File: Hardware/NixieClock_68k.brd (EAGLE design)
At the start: 100 x 100 mm, 70 parts, among them IC1 68008, IC10 7805, IC11 MIC803, IC2 AS6C1008, IC3 39SF020, IC4 DS1244Y, IC5 FT245R, IC6 NE555, IC7 ATF1504AS, IC8 74HC374N, IC9 74HC373N, X1 4MHz

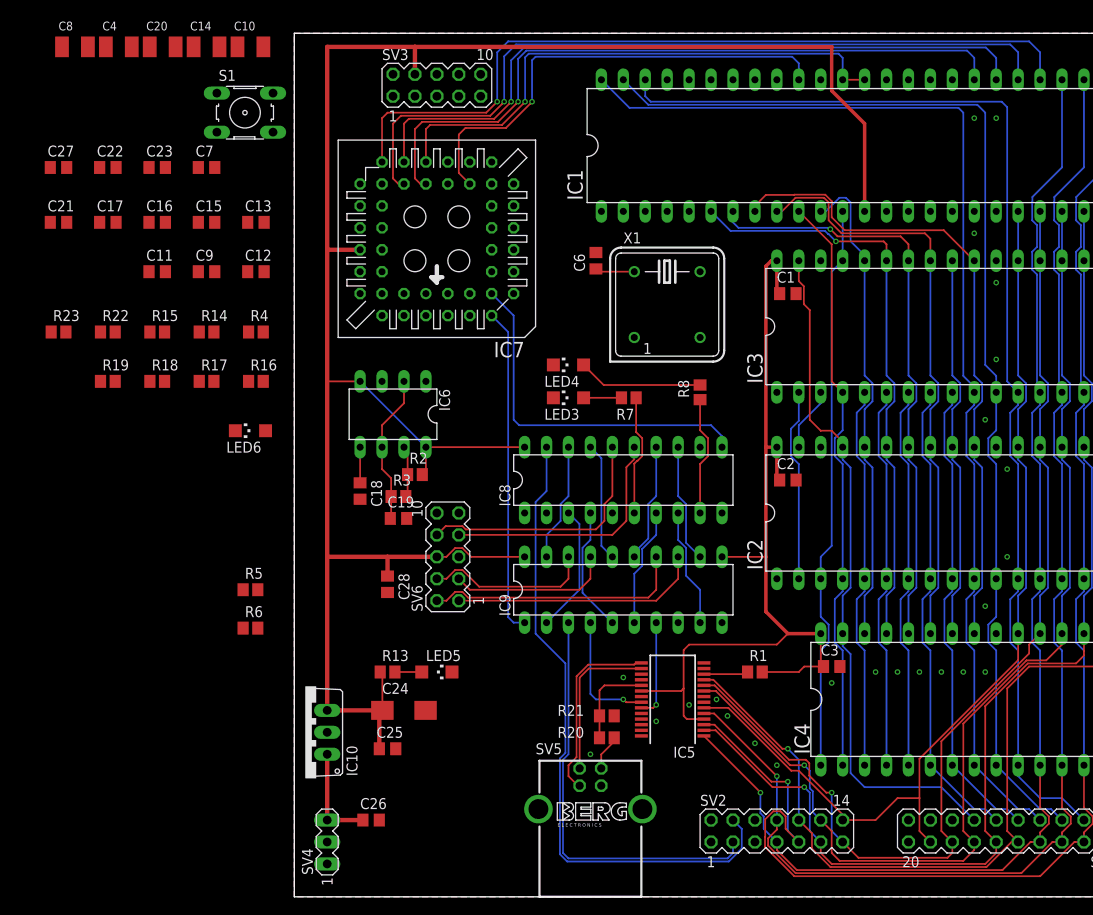
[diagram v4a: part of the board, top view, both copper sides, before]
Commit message: replaced cpld with ttl logic
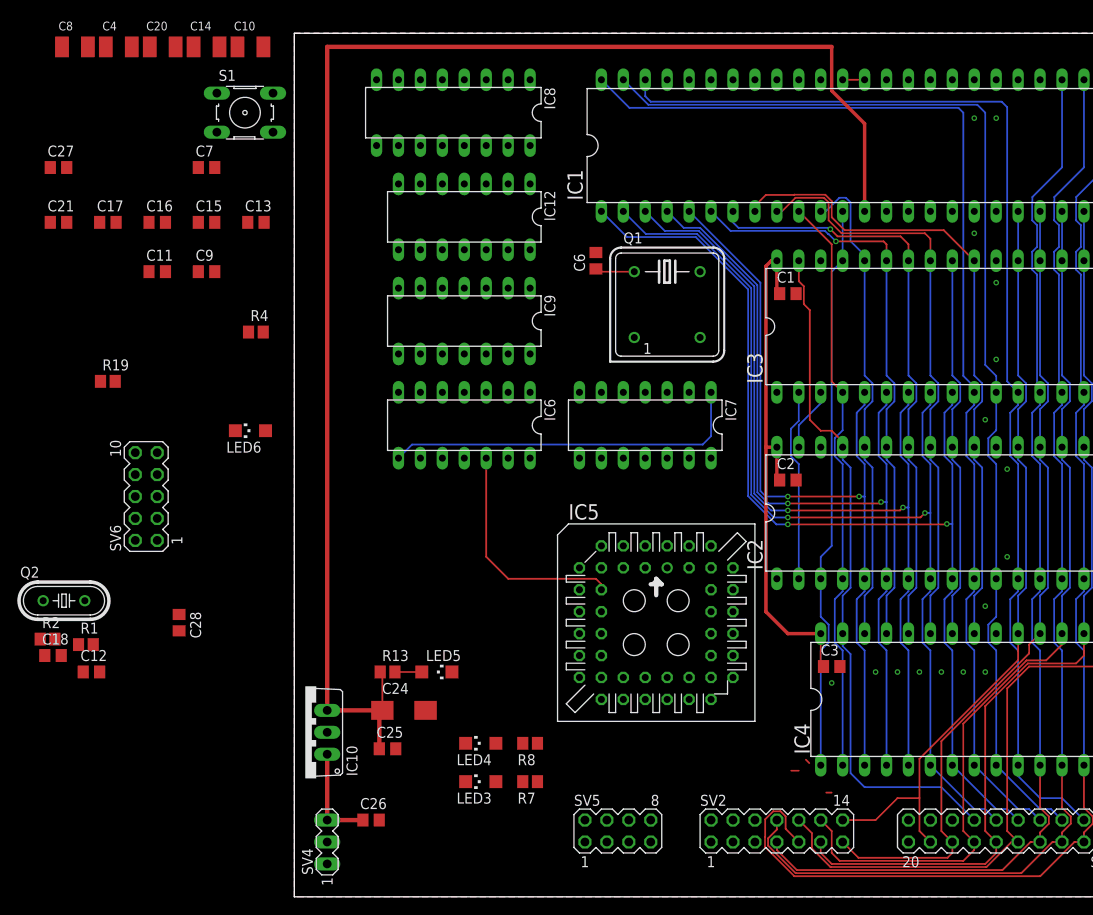
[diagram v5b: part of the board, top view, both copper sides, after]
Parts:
- removed C19: 47nF, rcl:C0805
- removed C22, C23: 100nF, rcl:C0805
- removed R14, R15, R16, R17, R18, R21, R22, R23, R5, R6: 10k, rcl:R2012
- removed R20: 4k7, rcl:R2012
- removed R3: 150k, rcl:R2012
- removed SV3: (no value), con-lstb:MA05-2
- added IC12: 74HC08N, 74xx-eu:DIL14
- added Q2: 3.6864MHz, crystal:HC49/S
- C12: value 100nF -> 27pF
- C18: value 10nF -> 27pF
- IC5: value FT245R -> 68681; device Parts:SSOP28 -> Parts:PLCC-S44
- IC6: value NE555 -> 74HC30N; device st-microelectronics:DIL-08 -> 74xx-eu:DIL14
- IC7: value ATF1504AS -> 74HC04N; device Parts:PLCC-S44 -> 74xx-eu:DIL14
- IC8: value 74HC374N -> 74HC138N; device 74xx-eu:DIL20 -> 74xx-eu:DIL16
- IC9: value 74HC373N -> 74HC266N; device 74xx-eu:DIL20 -> 74xx-eu:DIL14
- R1: value 10k -> 100R
- R2: value 4k7 -> 100R
- SV5: value PN61729-S -> (none); device con-berg:PN61729-S -> con-lstb:MA04-2
- moved R1 77.5 mm to (-24.1, 29.2)
- moved C12 50.1 mm to (-23.5, 26.0)
- moved IC8 46.9 mm to (18.4, 90.8), turned to 180 degrees
- moved R2 46.6 mm to (-28.6, 29.8)
- moved R7 45.9 mm to (27.3, 13.3)
- moved LED3 45.6 mm to (21.6, 13.3)
- moved R8 45.2 mm to (27.3, 17.8), turned to 180 degrees
- moved LED4 45.0 mm to (21.6, 17.8)
- moved C18 40.3 mm to (-27.9, 27.9), turned to 0 degrees
- moved IC9 36.2 mm to (19.7, 66.7), turned to 180 degrees
- moved SV6 35.6 mm to (-17.1, 46.4)
- moved IC7 32.4 mm to (40.6, 54.6)
- moved C28 24.5 mm to (-13.3, 31.8)
- moved IC5 9.09 mm to (41.9, 31.8), turned to 0 degrees
- moved IC6 8.35 mm to (19.7, 54.6)
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- renumbered X1 to Q1
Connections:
- removed net !BERR: IC1.40, R14.1
- removed net !BR: IC1.33, R18.1
- removed net !IO_IN_CS: IC7.6, IC9.1
- removed net !IO_OUT_CS: IC7.8, IC8.11
- removed net !USB_PWREN: IC5.12, R1.1
- removed net !USB_RD: IC5.13
- removed net !USB_RESET: IC5.19, R20.1, R21.2
- removed net !USB_RXF: IC5.23, IC9.7, R6.1
- removed net !USB_TXE: IC5.22, IC9.4, R5.1
- removed net !VFD_WR: SV2.5
- removed net !VPA: IC1.39, IC7.21, R22.1
- removed net 555_D: IC6.7, R2.1, R3.2
- removed net 555_T: C19.1, IC6.2, IC6.6, R3.1
- removed net CPLD_TCK: IC7.32, R17.1, SV3.1
- removed net CPLD_TDI: IC7.7, R16.1, SV3.9
- removed net CPLD_TDO: IC7.38, SV3.3
- removed net CPLD_TMS: IC7.13, R15.1, SV3.5
- removed net N$10: R20.2, SV5.1
- removed net N$12: IC7.18
- removed net N$13: IC7.19
- removed net N$14: IC7.20
- removed net N$21: IC7.29
- removed net N$22: IC7.31
- removed net N$23: IC7.33
- removed net N$24: IC7.34
- removed net N$25: IC7.36
- removed net N$26: IC7.37
- removed net N$27: IC7.39
- removed net N$28: IC7.40
- removed net N$29: IC7.1
- removed net N$30: IC7.44
- removed net N$31: IC7.41
- removed net N$32: IC7.4
- removed net N$33: IC7.5
- removed net N$36: IC7.9
- removed net N$37: IC7.11
- removed net N$38: IC7.12
- removed net TIMER_IRQ: IC6.3
- removed net USB+: IC5.15, SV5.3
- removed net USB-: IC5.16, SV5.2
- removed net USB_WR: IC5.14
- new net !68681_CS: IC5.39, IC8.13
- new net !68681_DTACK: IC5.10, IC6.12
- new net !68681_IACK: IC5.41, IC7.6
- new net !RAM_CS0: IC8.9, IC9.5
- new net !RAM_CS1: IC8.7, IC9.6
- new net !ROM_CS0: IC8.15, IC9.1
- new net !ROM_CS1: IC8.14, IC9.2
- new net !VFD_CS: IC6.11, IC8.10, SV2.5
- new net 68681_X1: IC5.36, R2.1
- new net 68681_X2: IC5.37, R1.2
- new net UART0_RX: IC5.35, SV5.2
- new net UART0_TX: IC5.33, SV5.1
- new net UART1_RX: IC5.11, SV5.4
- new net UART1_TX: IC5.13, SV5.3
- net !AS: now also IC8.5; no longer IC7.28
- net !DS: no longer IC7.27
- net !DTACK: now also IC7.2; no longer IC7.25, R23.1
- net !IPL1: now also IC5.24
- net !NIXIE_CS: now also IC6.3, IC8.11
- net !OE: now also IC7.4
- net !RAM_CS: now also IC6.5, IC9.4
- net !RESET: now also IC5.38; no longer IC7.24
- net !ROM_CS: now also IC6.4, IC9.3
- net !RTC_CS: now also IC6.6, IC8.12
- net !VFD_RESET: now also IC5.30; no longer IC8.19
- net +5V: now also IC1.33, IC1.39, IC1.40, IC12.14, IC5.44, IC6.1, IC6.14, IC6.2, IC7.14, IC8.16, IC8.6, IC9.14, SV5.6, SV5.8; no longer C22.1, C23.1, IC5.20, IC5.4, IC6.4, IC6.8, IC7.15, IC7.23, IC7.3, IC7.35, IC8.20, IC9.11, IC9.20, R1.2, R14.2, R15.2, R16.2, R18.2, R2.2, R22.2, R23.2, R6.2, SV3.4
- net A0: now also IC5.2
- net A1: now also IC5.4
- net A16: now also IC8.1
- net A17: now also IC8.2
- net A18: now also IC8.3
- net A2: now also IC5.6
- net A3: now also IC5.7
- net CLK: no longer IC7.43
- net D0: now also IC5.28; no longer IC5.1, IC8.3, IC9.2
- net D1: now also IC5.18; no longer IC5.5, IC8.4, IC9.5
- net D2: now also IC5.27; no longer IC5.3, IC8.7, IC9.6
- net D3: now also IC5.19; no longer IC5.11, IC8.8, IC9.9
- net D4: now also IC5.26; no longer IC5.2, IC8.13, IC9.12
- net D5: now also IC5.20; no longer IC5.9, IC8.14, IC9.15
- net D6: now also IC5.25; no longer IC5.10, IC8.17, IC9.16
- net D7: now also IC5.21; no longer IC5.6, IC8.18, IC9.19
- net FC0: now also IC12.5
- net FC1: now also IC12.4
- net FC2: now also IC12.1
- net GND: now also C12.2, IC12.7, IC5.22, IC6.7, IC7.7, IC8.4, IC8.8, IC9.7, SV5.5, SV5.7; no longer C12.1, C19.2, C22.2, C23.2, IC5.18, IC5.21, IC5.25, IC5.26, IC5.7, IC6.1, IC7.10, IC7.22, IC7.30, IC7.42, IC8.1, IC8.10, IC9.10, IC9.8, R17.2, R21.1, R5.2, SV3.10, SV5.4, SV5.S1, SV5.S2
- net N$1: now also C12.1, Q2.2, R1.1; no longer C12.2, IC5.17
- net N$11: now also IC12.2, IC12.6; no longer IC7.14
- net N$2: now also Q2.1, R2.2; no longer IC6.5
- net N$3: now also IC6.8, IC7.1; no longer IC7.17
- net N$5: now also IC12.3, IC7.5; no longer IC7.16
- net OUT0: no longer IC8.16
- net OUT1: no longer IC8.15
- net R/!W!: now also IC5.9, IC7.3; no longer IC7.26
- net STATUS0: now also IC5.32; no longer IC8.2
- net STATUS1: now also IC5.14, R7.1; no longer IC8.5
- net STATUS2: now also IC5.31; no longer IC8.6, R7.1
- net STATUS3: now also IC5.15; no longer IC8.9
- net SW0: now also IC5.8; no longer IC9.13
- net SW1: now also IC5.5; no longer IC9.14
- net SW2: now also IC5.40; no longer IC9.17
- net SW3: now also IC5.43; no longer IC9.18
- net VFD_BUSY: now also IC5.3; no longer IC9.3
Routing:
- net +5V: track 340.9 -> 238.2 mm
- net !AS: track 92.0 -> 0.00 mm, vias 1 -> 0
- net !DS: track 90.7 -> 0.00 mm, vias 1 -> 0
- net R/!W!: track 163.7 -> 81.2 mm, vias 1 -> 0
- net !DTACK: track 81.6 -> 0.00 mm, vias 1 -> 0
- net !VFD_RESET: track 75.1 -> 0.00 mm
- net A3: track 54.9 -> 124.6 mm, vias 0 -> 2
- net A4: track 54.9 -> 119.4 mm, vias 0 -> 2
- net !RESET: track 64.0 -> 2.54 mm, vias 1 -> 0
- net A5: track 44.7 -> 103.7 mm, vias 0 -> 2
- net !VPA: track 54.4 -> 0.00 mm, vias 1 -> 0
- net A6: track 44.7 -> 98.2 mm, vias 0 -> 2
- net VFD_BUSY: track 48.4 -> 0.00 mm
- net A7: track 44.7 -> 92.8 mm, vias 0 -> 2
- net N$3: track 0.00 -> 42.3 mm
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
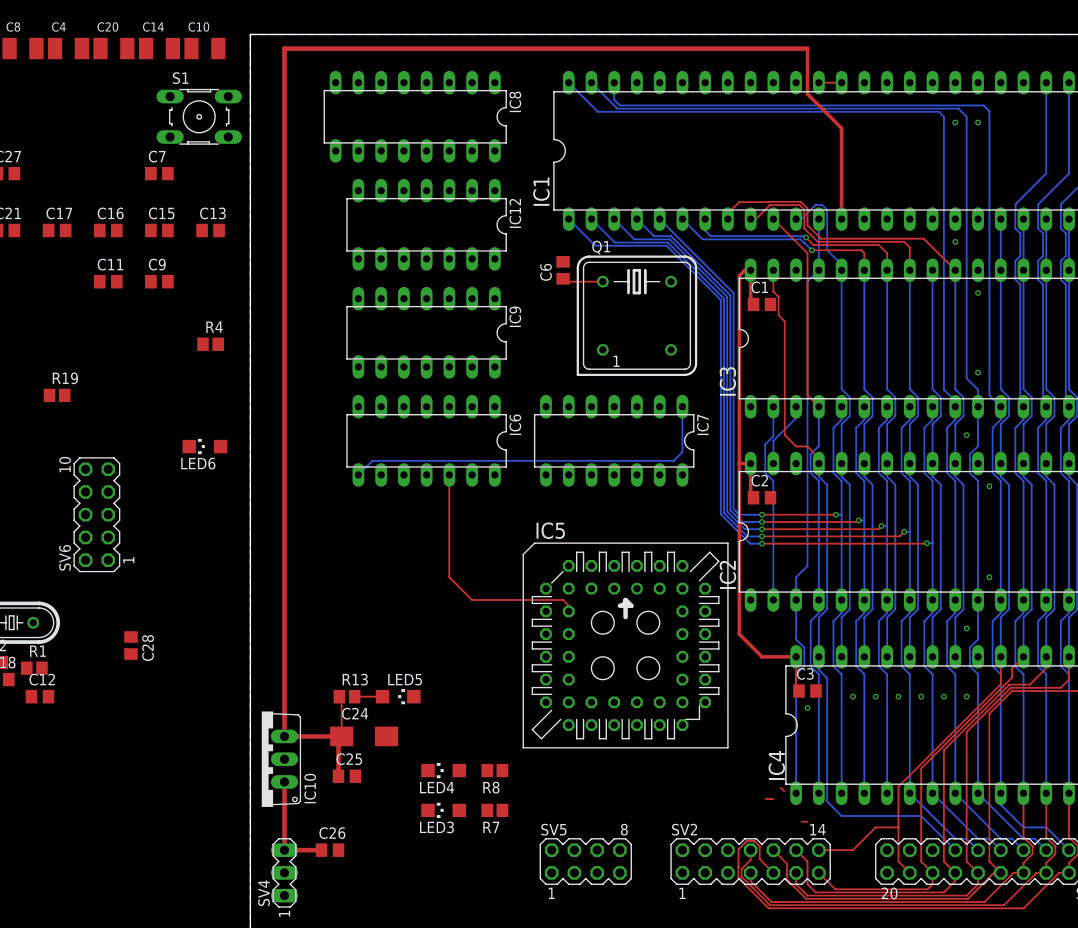
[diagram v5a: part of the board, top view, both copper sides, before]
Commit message: routed most system control signals
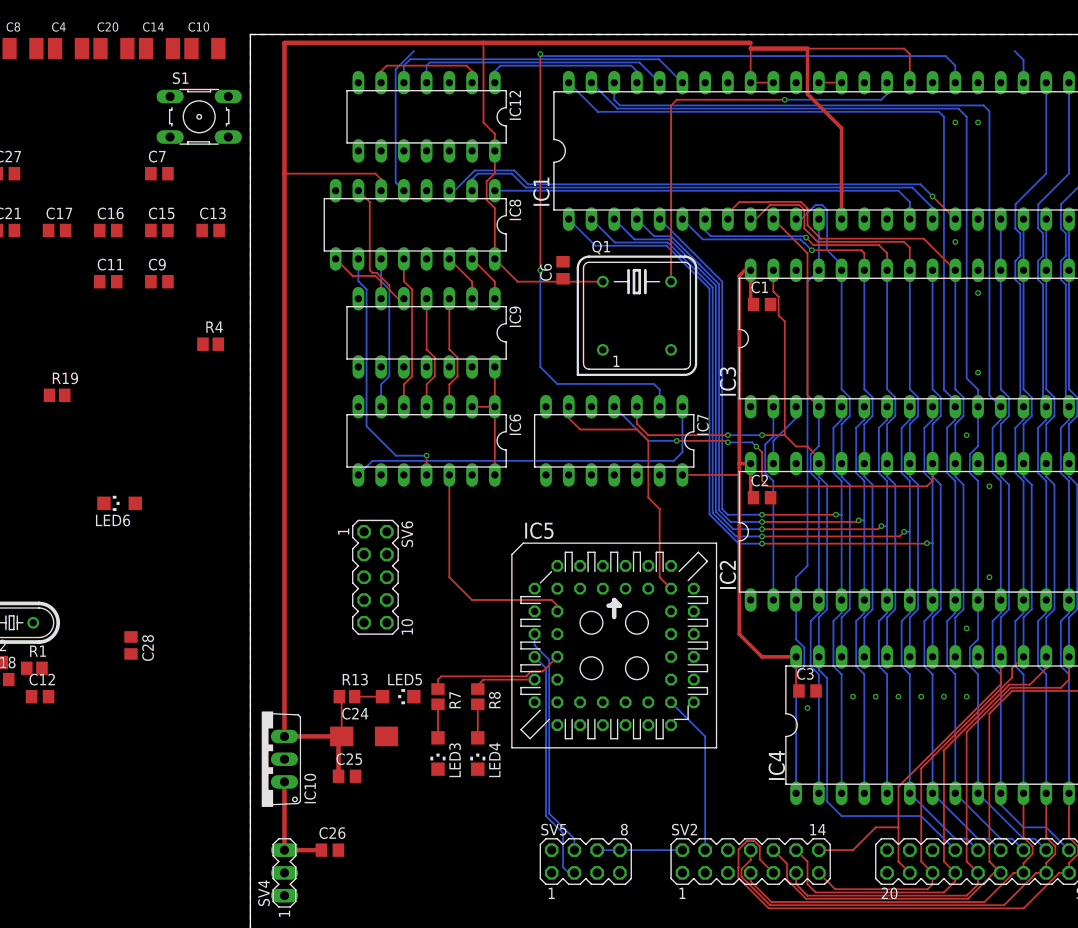
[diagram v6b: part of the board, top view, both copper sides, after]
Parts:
- moved SV6 31.9 mm to (14.0, 39.4), turned to 270 degrees
- moved R7 14.2 mm to (21.0, 26.0), turned to 270 degrees
- moved IC12 12.1 mm to (19.7, 90.8)
- moved IC8 12.1 mm to (18.4, 78.7)
- moved LED6 11.4 mm to (-14.6, 47.6)
- moved R8 8.47 mm to (25.4, 26.0), turned to 270 degrees
- moved LED3 6.38 mm to (21.0, 19.7), turned to 180 degrees
- moved LED4 4.26 mm to (25.4, 19.7), turned to 180 degrees
- moved IC5 1.27 mm to (40.6, 31.8)
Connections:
- net !NIXIE_CS: now also IC6.6; no longer IC6.3
- net !RAM_CS: now also IC6.4; no longer IC6.5
- net !RAM_CS0: now also IC9.6; no longer IC9.5
- net !RAM_CS1: now also IC9.5; no longer IC9.6
- net !ROM_CS: now also IC6.3; no longer IC6.4
- net !RTC_CS: now also IC6.5; no longer IC6.6
- net FC0: now also IC12.1; no longer IC12.5
- net FC2: now also IC12.5; no longer IC12.1
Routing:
- net !DTACK: track 0.00 -> 100.0 mm, vias 0 -> 2
- net +5V: track 238.2 -> 337.6 mm
- net A18: track 0.00 -> 59.7 mm, vias 0 -> 1
- net A17: track 0.00 -> 55.8 mm
- net A16: track 22.3 -> 71.1 mm
- net CLK: track 0.00 -> 45.6 mm, vias 0 -> 1
- net !OE: track 44.7 -> 88.0 mm, vias 0 -> 3
- net FC2: track 0.00 -> 34.4 mm
- net !VFD_CS: track 0.00 -> 29.3 mm, vias 0 -> 1
- net FC1: track 0.00 -> 29.0 mm
- net !68681_IACK: track 0.00 -> 28.8 mm
- net UART1_TX: track 0.00 -> 26.3 mm
- net UART1_RX: track 0.00 -> 26.0 mm
- net !AS: track 0.00 -> 20.8 mm
- net FC0: track 0.00 -> 18.9 mm
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
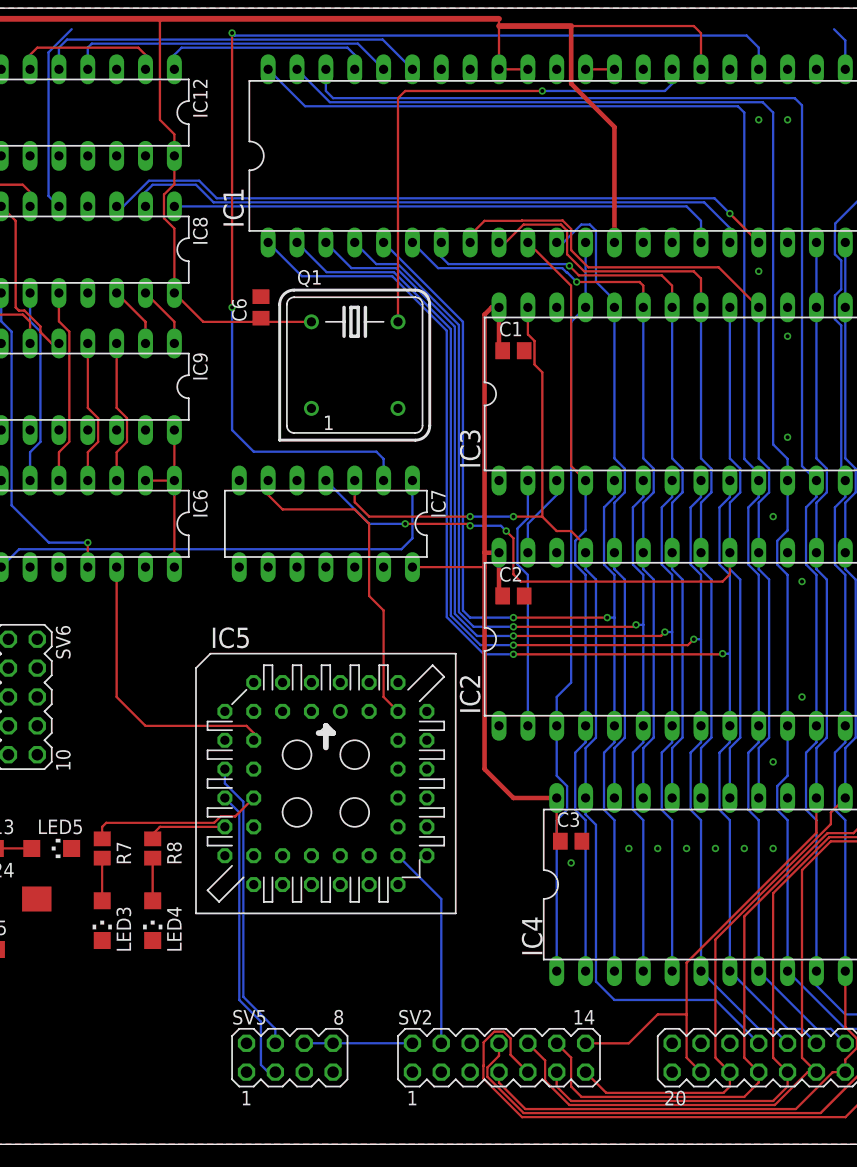
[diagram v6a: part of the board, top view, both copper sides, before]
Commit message: routed 68681 data bus, some chip selects
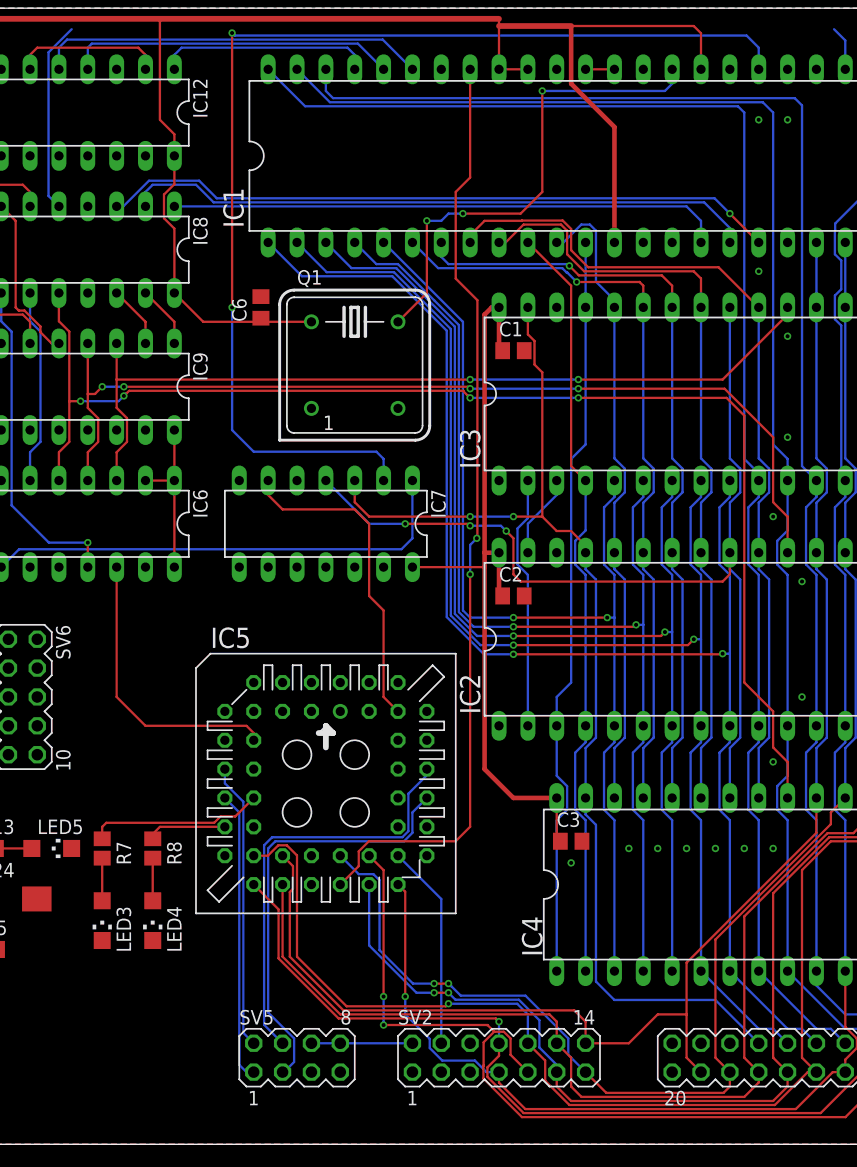
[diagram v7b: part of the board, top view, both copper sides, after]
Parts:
- moved SV5 0.63 mm to (38.1, 7.62)
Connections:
- net UART0_RX: now also SV5.4; no longer SV5.2
- net UART0_TX: now also SV5.3; no longer SV5.1
- net UART1_RX: now also SV5.2; no longer SV5.4
- net UART1_TX: now also SV5.1; no longer SV5.3
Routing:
- net !RTC_CS: track 17.3 -> 113.2 mm, vias 0 -> 4
- net !IPL1: track 0.00 -> 82.5 mm, vias 0 -> 2
- net !RAM_CS: track 12.8 -> 85.9 mm, vias 0 -> 4
- net !ROM_CS: track 12.8 -> 74.9 mm, vias 0 -> 2
- net D7: track 89.7 -> 129.4 mm
- net D3: track 114.2 -> 152.8 mm, vias 0 -> 1
- net UART0_TX: track 0.00 -> 38.0 mm
- net UART0_RX: track 0.00 -> 37.4 mm
- net D5: track 103.8 -> 138.6 mm
- net D6: track 94.8 -> 128.7 mm, vias 0 -> 2
- net D1: track 133.1 -> 164.1 mm, vias 0 -> 1
- net D4: track 107.0 -> 135.3 mm, vias 0 -> 2
- net D2: track 142.7 -> 168.1 mm, vias 0 -> 2
- net D0: track 126.6 -> 149.1 mm, vias 0 -> 1
- net CLK: track 45.6 -> 43.0 mm, vias 1 -> 3
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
